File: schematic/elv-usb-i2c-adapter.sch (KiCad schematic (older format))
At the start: 14 parts, among them IC1 ATmega88PA-AU, IC3 74HC14

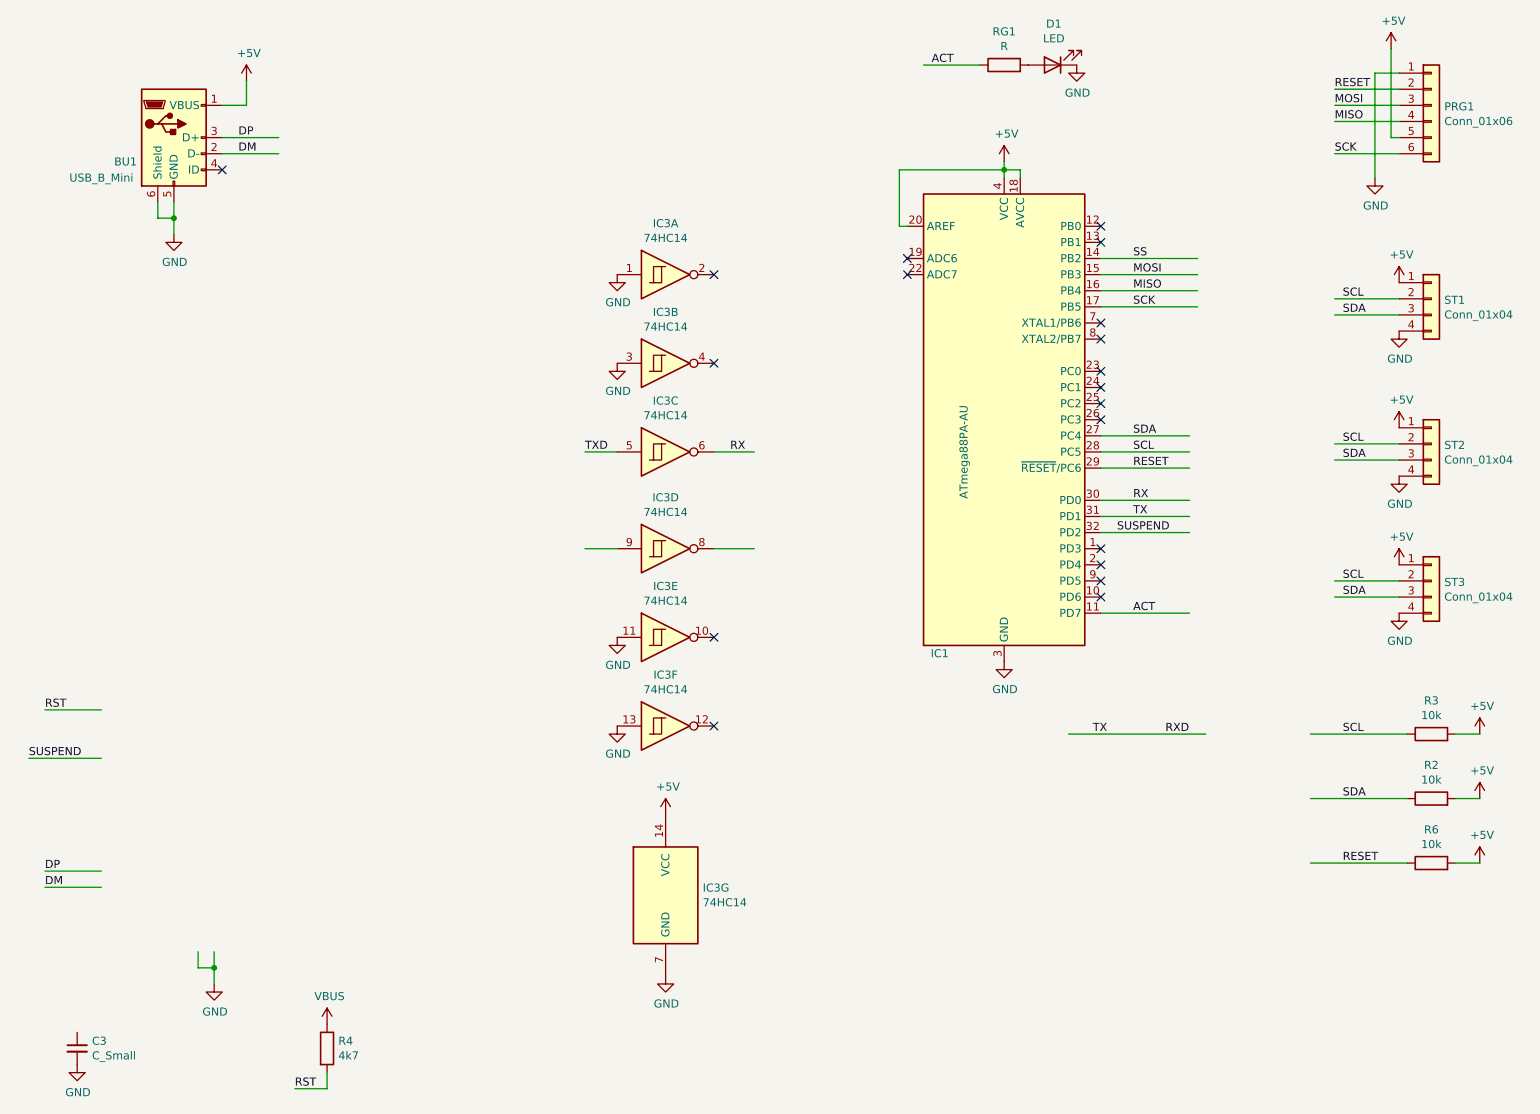
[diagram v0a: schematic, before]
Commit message: Added CP2102
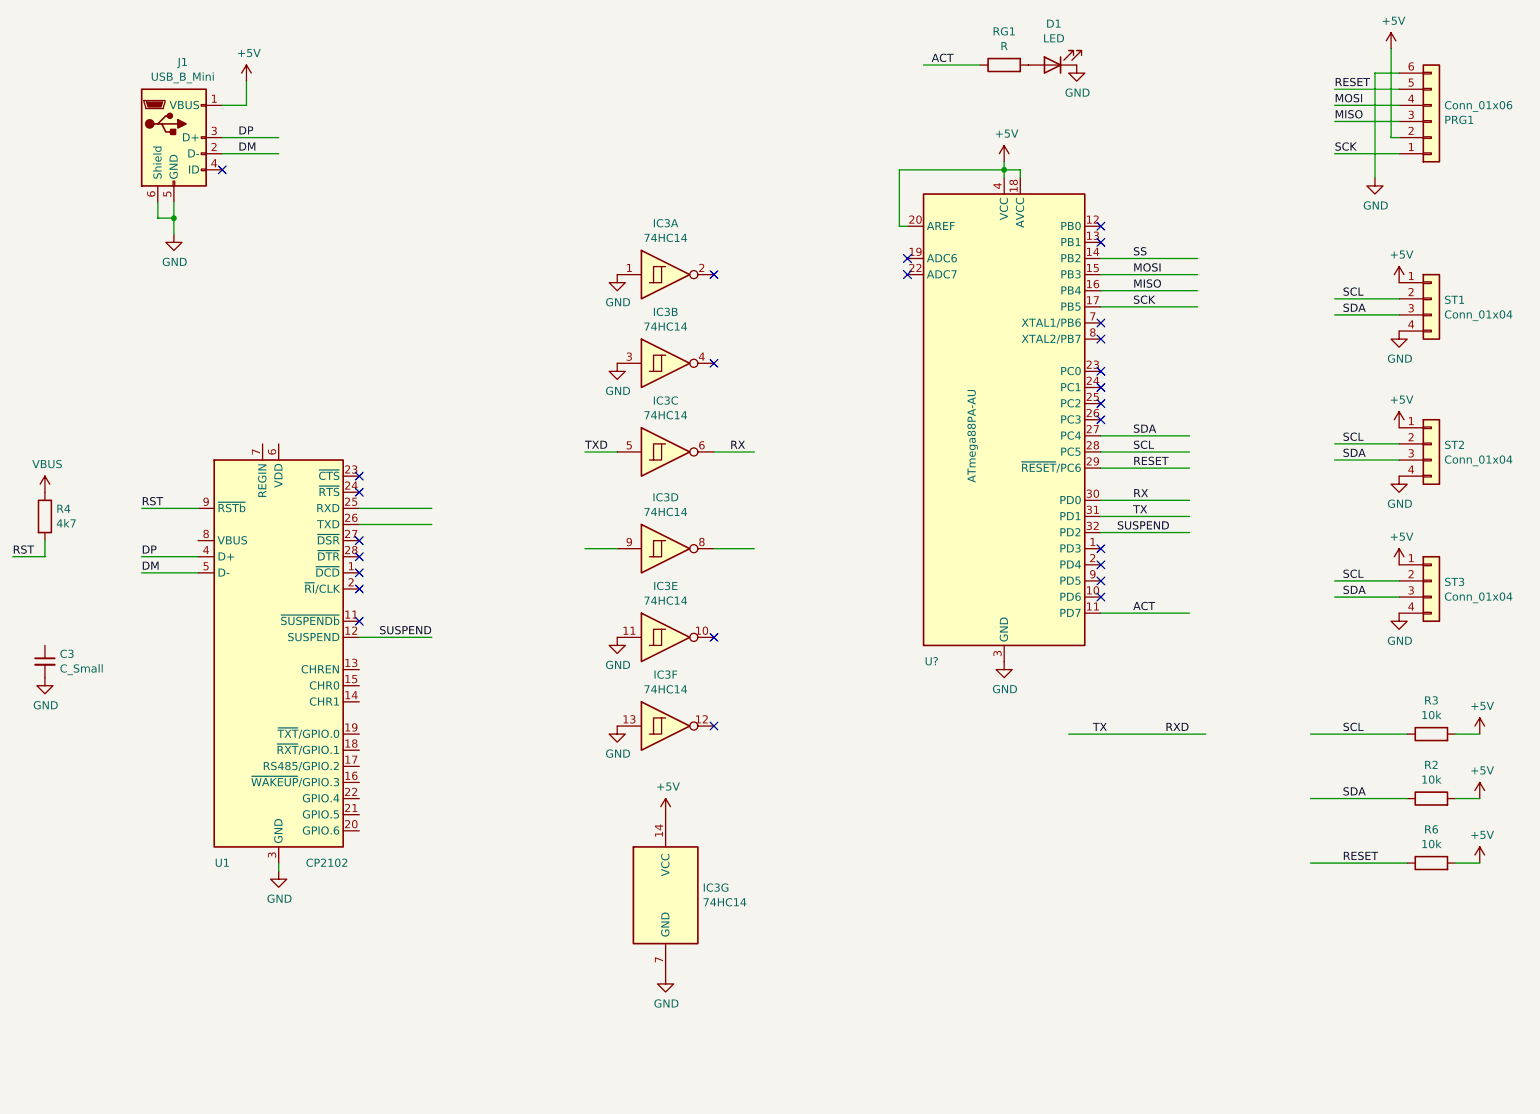
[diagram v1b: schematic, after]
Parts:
- removed BU1: USB_B_Mini, symbol Connector:USB_B_Mini
- removed IC1: ATmega88PA-AU, Package_QFP:TQFP-32_7x7mm_P0.8mm, symbol MCU_Microchip_ATmega:ATmega88PA-AU
- added J1: USB_B_Mini, Connector_USB:USB_Mini-B_Wuerth_65100516121_Horizontal, symbol Connector:USB_B_Mini
- added U1: CP2102, Package_DFN_QFN:QFN-28-1EP_5x5mm_P0.5mm_EP3.35x3.35mm, symbol Interface_USB:CP2102N-A01-GQFN28
- added U?: ATmega88PA-AU, Package_QFP:TQFP-32_7x7mm_P0.8mm, symbol MCU_Microchip_ATmega:ATmega88PA-AU
- IC3: footprint (none) -> Package_SO:SOIC-14_3.9x8.7mm_P1.27mm
- PRG1: footprint (none) -> Connector_PinHeader_2.54mm:PinHeader_1x06_P2.54mm_Vertical
- ST1, ST2, ST3: footprint (none) -> Connector_PinHeader_2.54mm:PinHeader_1x04_P2.54mm_Vertical
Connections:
- wire segments 62 -> 61
- no-connect marks 19 -> 26
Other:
- moved on the sheet: C3, R4
